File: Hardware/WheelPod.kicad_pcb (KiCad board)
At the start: 2 copper layers, 25.4 x 25.4 mm, 9 parts, among them U1 PIC32MX250F128D, U2 LDC1000

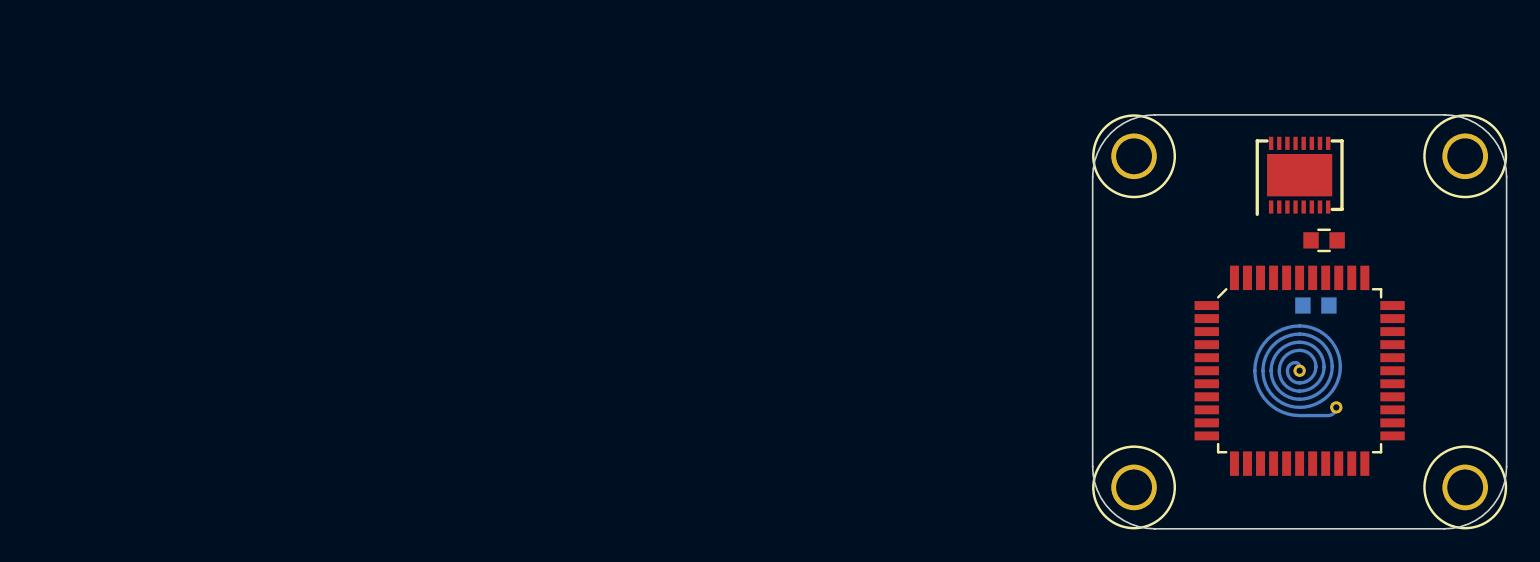
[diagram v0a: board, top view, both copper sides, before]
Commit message: Split into separate boards
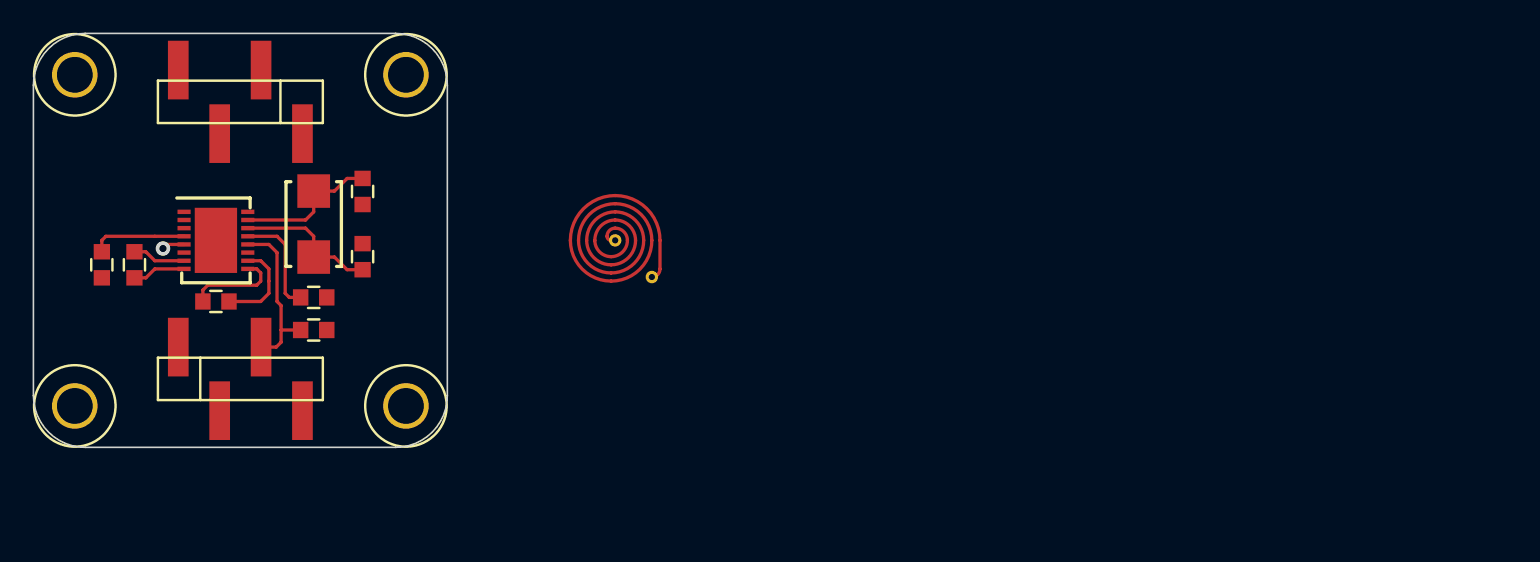
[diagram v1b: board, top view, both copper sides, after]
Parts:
- removed the MECH-HOLE220 at (199.8, 129.8)
- removed the MECH-HOLE220 at (220.2, 129.8)
- removed the MECH-HOLE220 at (220.2, 150.2)
- removed the MECH-HOLE220 at (199.8, 150.2)
- removed U2: LDC1000, SON50P500X400-17N
- added C3: 0.1uF, CAPC1608-N, F.Cu at (149.5, 140.5)
- added C4: C, CAPC1608-N, F.Cu at (138.5, 136.5)
- added C5: 0.056uF, CAPC1608-N, F.Cu at (149.5, 138.5)
- added C6: 20pF, CAPC1608-N, F.Cu at (152.5, 136.0)
- added C7: 20pF, CAPC1608-N, F.Cu at (152.5, 132.0)
- added J1: CONN-4, HDRV4W38P254_4X1-SMT, F.Cu at (145.0, 143.5)
- added J2: CONN-4, HDRV4W38P254_4X1-SMT, F.Cu at (145.0, 126.5)
- added MECH-HOLE220: VAL**, MECH-HOLE220, F.Cu at (134.8, 124.8)
- added MECH-HOLE220: VAL**, MECH-HOLE220, F.Cu at (155.2, 124.8)
- added MECH-HOLE220: VAL**, MECH-HOLE220, F.Cu at (155.2, 145.2)
- added MECH-HOLE220: VAL**, MECH-HOLE220, F.Cu at (134.8, 145.2)
- added X1: 8MHz, XTAL-2SMD-50X32, F.Cu at (149.5, 134.0)
- C1, L1: moved to F.Cu
- C2: value C -> 0.1uF
- U1: value PIC32MX250F128D -> LDC1000; footprint QFP80P1200x1200-44N -> SON50P500X400-17N
- moved C2 75.0 mm to (136.5, 136.5), turned to 270 degrees
- moved C1 67.5 mm to (143.5, 138.8), turned to 0 degrees
- moved U1 67.0 mm to (143.5, 135.0), turned to 270 degrees
- moved L1 42.8 mm to (168.0, 135.0), turned to 0 degrees
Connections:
- C1 pad 1: N-000008 -> N-0000012
- C1 pad 2: N-0000019 -> N-0000011
- C2 pad 1: N-0000018 -> +3.3V
- C2 pad 2: N-000009 -> GND
- L1 pad 1: N-0000019 -> N-0000011
- L1 pad 2: N-000008 -> N-0000012
- U1 pad 1: (no net) -> /SCK
- U1 pad 10: (no net) -> N-0000011
- U1 pad 11: (no net) -> GND
- U1 pad 12: (no net) -> +5V
- U1 pad 13: (no net) -> N-0000015
- U1 pad 14: (no net) -> /XIN
- U1 pad 15: (no net) -> /XOUT
- U1 pad 16: (no net) -> /INT
- U1 pad 17: (no net) -> GND
- U1 pad 2: (no net) -> /CS
- U1 pad 3: (no net) -> /MOSI
- U1 pad 4: (no net) -> +3.3V
- U1 pad 5: (no net) -> /MISO
- U1 pad 6: (no net) -> GND
- U1 pad 7: (no net) -> N-0000013
- U1 pad 8: (no net) -> N-0000014
- U1 pad 9: (no net) -> N-0000012
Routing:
- net +5V: track 0.00 -> 10.2 mm
- net /XOUT: track 0.00 -> 8.85 mm
- net /XIN: track 0.00 -> 8.85 mm
- net N-0000015: track 0.00 -> 6.56 mm
- net N-0000012: track 0.00 -> 5.88 mm
- net +3.3V: track 0.00 -> 5.85 mm
- net N-0000011: track 0.00 -> 5.66 mm
- net N-0000014: track 0.00 -> 3.27 mm
- net N-0000013: track 0.00 -> 3.27 mm
- net /MISO: track 0.00 -> 1.40 mm, vias 0 -> 1
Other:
- outline, holes or cut-outs redrawn
- net class Default: clearance 0.254 -> 0.2032; trace_width 0.254 -> 0.2032
- rule trace_clearance: 0.254 -> 0.2032
- rule trace_min: 0.254 -> 0.2032
